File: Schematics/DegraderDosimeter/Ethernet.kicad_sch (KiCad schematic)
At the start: 38 parts, among them J1 RJ45_Amphenol_RJMG1BD3B8K1ANR, U1 LAN8742A, U2 USBLC6-4SC6, U3 H1102NL, Y1 Crystal

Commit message: Set Ethernet PHY crystal value to 25.000 MHz
Y1 carried the generic "Crystal" value with no frequency. The LAN8742A
RMII reference design clocks the PHY from a 25 MHz crystal (X4,
X53T-C20SSA25.000MHz on the ST Nucleo-144 MB1137/MB1364 boards), from
which the PHY derives the 50 MHz RMII_REF_CLK for the MCU. The 30 pF
load capacitors already match.

Co-Authored-By: Claude Opus 5 <noreply@anthropic.com>
Claude-Session: https://claude.ai/code/session_01Ej9hevrS5JU2uwVi6UHQUS
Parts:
- Y1: value Crystal -> 25.000MHz
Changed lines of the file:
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@@
 			)
 		)
-		(property "Value" "Crystal"
+		(property "Value" "25.000MHz"
 			(at 49.234 127.2539 90)
 			(show_name no)

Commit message: Align Ethernet passives with MB1364-H723ZG BOM and fix footprints
Every passive on the sheet carried Capacitor_SMD:C_1206_3216Metric,
including all 22 resistors. Assign real packages matching the
NUCLEO-H723ZG BOM (MB1364-H723ZG-E01), which uses 0402 throughout:

  R1-R22   -> Resistor_SMD:R_0402_1005Metric   (RC0402FR-07* series)
  C1-C9    -> Capacitor_SMD:C_0402_1005Metric
  C10      -> kept at 1206; the 1nF Bob Smith cap is 2kV rated
              (CC1206KKX7RDBB102) and genuinely is a 1206 part
  FB1      -> Inductor_SMD:L_0603_1608Metric   (FCM1608KF-601T03)

Two value corrections from the same BOM:

  R12-R15  50 -> 49R9   centre-tap termination is RC0402FR-0749R9L
  C1, C2   30p -> 5.6p  X4 is an NDK NX2016SA 25MHz 6pF-load crystal,
                        loaded with 5.6pF (CC0402BRNPO9BN5R6), not the
                        30pF used with the older MB1137 crystal

ERC violation count is unchanged at 1445, so no new violations.

Co-Authored-By: Claude Opus 5 <noreply@anthropic.com>
Claude-Session: https://claude.ai/code/session_01Ej9hevrS5JU2uwVi6UHQUS
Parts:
- C1, C2: value 30p -> 5.6p; footprint Capacitor_SMD:C_1206_3216Metric -> Capacitor_SMD:C_0402_1005Metric
- C3, C4, C5, C6, C7, C8, C9: footprint Capacitor_SMD:C_1206_3216Metric -> Capacitor_SMD:C_0402_1005Metric
- FB1: footprint Ferrite_THT:LairdTech_28C0236-0JW-10 -> Inductor_SMD:L_0603_1608Metric
- R1, R10, R11, R16, R17, R18, R19, R2, R20, R21, R22, R3, R4, R5, R6, R7, R8, R9: footprint Capacitor_SMD:C_1206_3216Metric -> Resistor_SMD:R_0402_1005Metric
- R12, R13, R14, R15: value 50 -> 49R9; footprint Capacitor_SMD:C_1206_3216Metric -> Resistor_SMD:R_0402_1005Metric
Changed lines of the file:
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@@
 			)
 		)
-		(property "Footprint" "Capacitor_SMD:C_1206_3216Metric"
+		(property "Footprint" "Resistor_SMD:R_0402_1005Metric"
 			(at 208.026 113.538 0)
 			(hide yes)
@@
 			)
 		)
-		(property "Footprint" "Capacitor_SMD:C_1206_3216Metric"
+		(property "Footprint" "Resistor_SMD:R_0402_1005Metric"
 			(at 33.528 65.024 0)
 			(hide yes)
@@
 			)
 		)
-		(property "Footprint" "Capacitor_SMD:C_1206_3216Metric"
+		(property "Footprint" "Resistor_SMD:R_0402_1005Metric"
 			(at 193.04 113.538 0)
 			(hide yes)
@@
 			)
 		)
-		(property "Footprint" "Capacitor_SMD:C_1206_3216Metric"
+		(property "Footprint" "Capacitor_SMD:C_0402_1005Metric"
 			(at 63.5 39.8272 0)
 			(hide yes)
@@
 			)
 		)
-		(property "Value" "50"
+		(property "Value" "49R9"
 			(at 154.94 36.068 0)
 			(show_name no)
@@
 			)
 		)
-		(property "Footprint" "Capacitor_SMD:C_1206_3216Metric"
+		(property "Footprint" "Resistor_SMD:R_0402_1005Metric"
 			(at 158.242 34.544 0)
 			(hide yes)
@@
 			)
 		)
-		(property "Footprint" "Capacitor_SMD:C_1206_3216Metric"
+		(property "Footprint" "Capacitor_SMD:C_0402_1005Metric"
 			(at 63.5 20.0152 0)
 			(hide yes)
@@
 			)
 		)
-		(property "Value" "30p"
+		(property "Value" "5.6p"
 			(at 34.036 122.682 90)
 			(show_name no)
@@
 			)
 		)
-		(property "Footprint" "Capacitor_SMD:C_1206_3216Metric"
+		(property "Footprint" "Capacitor_SMD:C_0402_1005Metric"
 			(at 37.592 117.3988 0)
 			(hide yes)
@@
 			)
 		)
-		(property "Value" "30p"
+		(property "Value" "5.6p"
 			(at 33.782 138.176 90)
 			(show_name no)
@@
 			)
 		)
-		(property "Footprint" "Capacitor_SMD:C_1206_3216Metric"
+		(property "Footprint" "Capacitor_SMD:C_0402_1005Metric"
 			(at 37.592 133.1468 0)
 			(hide yes)
@@
 			)
 		)
-		(property "Footprint" "Capacitor_SMD:C_1206_3216Metric"
+		(property "Footprint" "Resistor_SMD:R_0402_1005Metric"
 			(at 33.528 68.072 0)
 			(hide yes)
@@
 			)
 		)
-		(property "Footprint" "Capacitor_SMD:C_1206_3216Metric"
+		(property "Footprint" "Resistor_SMD:R_0402_1005Metric"
 			(at 47.498 44.45 0)
 			(hide yes)
@@
 			)
 		)
-		(property "Footprint" "Ferrite_THT:LairdTech_28C0236-0JW-10"
+		(property "Footprint" "Inductor_SMD:L_0603_1608Metric"
 			(at 204.724 23.114 90)
 			(hide yes)
@@
 			)
 		)
-		(property "Footprint" "Capacitor_SMD:C_1206_3216Metric"
+		(property "Footprint" "Resistor_SMD:R_0402_1005Metric"
 			(at 40.386 44.45 0)
 			(hide yes)
@@
 			)
 		)
-		(property "Footprint" "Capacitor_SMD:C_1206_3216Metric"
+		(property "Footprint" "Resistor_SMD:R_0402_1005Metric"
 			(at 33.782 72.898 0)
 			(hide yes)
@@
 			)
 		)
-		(property "Footprint" "Capacitor_SMD:C_1206_3216Metric"
+		(property "Footprint" "Resistor_SMD:R_0402_1005Metric"
 			(at 271.018 106.426 0)
 			(hide yes)
@@
 			)
 		)
-		(property "Footprint" "Capacitor_SMD:C_1206_3216Metric"
+		(property "Footprint" "Resistor_SMD:R_0402_1005Metric"
 			(at 54.864 73.914 0)
 			(hide yes)
@@
 			)
 		)
-		(property "Value" "50"
+		(property "Value" "49R9"
 			(at 133.858 36.322 0)
 			(show_name no)
@@
 			)
 		)
-		(property "Footprint" "Capacitor_SMD:C_1206_3216Metric"
+		(property "Footprint" "Resistor_SMD:R_0402_1005Metric"
 			(at 137.16 34.798 0)
 			(hide yes)
@@
 			)
 		)
-		(property "Footprint" "Capacitor_SMD:C_1206_3216Metric"
+		(property "Footprint" "Resistor_SMD:R_0402_1005Metric"
 			(at 105.664 78.994 0)
 			(hide yes)
@@
 			)
 		)
-		(property "Value" "50"
+		(property "Value" "49R9"
 			(at 148.336 36.068 0)
 			(show_name no)
@@
 			)
 		)
-		(property "Footprint" "Capacitor_SMD:C_1206_3216Metric"
+		(property "Footprint" "Resistor_SMD:R_0402_1005Metric"
 			(at 151.638 34.544 0)
 			(hide yes)
@@
 			)
 		)
-		(property "Footprint" "Capacitor_SMD:C_1206_3216Metric"
+		(property "Footprint" "Resistor_SMD:R_0402_1005Metric"
 			(at 20.32 81.28 0)
 			(hide yes)
@@
 			)
 		)
-		(property "Footprint" "Capacitor_SMD:C_1206_3216Metric"
+		(property "Footprint" "Capacitor_SMD:C_0402_1005Metric"
 			(at 63.5 30.1752 0)
 			(hide yes)
@@
 			)
 		)
-		(property "Footprint" "Capacitor_SMD:C_1206_3216Metric"
+		(property "Footprint" "Capacitor_SMD:C_0402_1005Metric"
 			(at 102.8192 44.958 0)
 			(hide yes)
@@
 			)
 		)
-		(property "Footprint" "Capacitor_SMD:C_1206_3216Metric"
+		(property "Footprint" "Resistor_SMD:R_0402_1005Metric"
 			(at 185.42 113.538 0)
 			(hide yes)
@@
 			)
 		)
-		(property "Footprint" "Capacitor_SMD:C_1206_3216Metric"
+		(property "Footprint" "Resistor_SMD:R_0402_1005Metric"
 			(at 200.66 113.538 0)
 			(hide yes)
@@
 			)
 		)
-		(property "Footprint" "Capacitor_SMD:C_1206_3216Metric"
+		(property "Footprint" "Resistor_SMD:R_0402_1005Metric"
 			(at 257.556 103.886 0)
 			(hide yes)
@@
 			)
 		)
-		(property "Footprint" "Capacitor_SMD:C_1206_3216Metric"
+		(property "Footprint" "Capacitor_SMD:C_0402_1005Metric"
 			(at 122.8852 44.958 0)
 			(hide yes)
@@
 			)
 		)
-		(property "Footprint" "Capacitor_SMD:C_1206_3216Metric"
+		(property "Footprint" "Capacitor_SMD:C_0402_1005Metric"
 			(at 112.9792 44.704 0)
 			(hide yes)
@@
 			)
 		)
-		(property "Footprint" "Capacitor_SMD:C_1206_3216Metric"
+		(property "Footprint" "Resistor_SMD:R_0402_1005Metric"
 			(at 20.32 97.282 0)
 			(hide yes)
@@
 			)
 		)
-		(property "Footprint" "Capacitor_SMD:C_1206_3216Metric"
+		(property "Footprint" "Resistor_SMD:R_0402_1005Metric"
 			(at 36.576 105.664 0)
 			(hide yes)
@@
 			)
 		)
-		(property "Footprint" "Capacitor_SMD:C_1206_3216Metric"
+		(property "Footprint" "Resistor_SMD:R_0402_1005Metric"
 			(at 257.556 93.726 0)
 			(hide yes)
@@
 			)
 		)
-		(property "Value" "50"
+		(property "Value" "49R9"
 			(at 141.224 36.322 0)
 			(show_name no)
@@
 			)
 		)
-		(property "Footprint" "Capacitor_SMD:C_1206_3216Metric"
+		(property "Footprint" "Resistor_SMD:R_0402_1005Metric"
 			(at 144.526 34.798 0)
 			(hide yes)
@@
 			)
 		)
-		(property "Footprint" "Capacitor_SMD:C_1206_3216Metric"
+		(property "Footprint" "Resistor_SMD:R_0402_1005Metric"
 			(at 54.102 44.45 0)
 			(hide yes)
@@
 			)
 		)
-		(property "Footprint" "Capacitor_SMD:C_1206_3216Metric"
+		(property "Footprint" "Capacitor_SMD:C_0402_1005Metric"
 			(at 221.4372 35.306 0)
 			(hide yes)

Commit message: Set Ethernet ferrite bead value to 600R@100MHz
FB1 carried the placeholder value "FerriteBead_Small" with no impedance
specified. It matches L1 on the MB1364 Ethernet sheet, which feeds the
PHY supply from 3V3 and is a TAI-TECH FCM1608KF-601T03, 600R@100MHz
+/-25%, 350mA, 0603. The 0603 footprint set in the previous commit is
already correct for that part.

Co-Authored-By: Claude Opus 5 <noreply@anthropic.com>
Claude-Session: https://claude.ai/code/session_01Ej9hevrS5JU2uwVi6UHQUS
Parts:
- FB1: value FerriteBead_Small -> 600R@100MHz
- R1: value R_Small_US -> 33
- Y1: footprint Crystal:Crystal_SMD_Abracon_ABM10-4Pin_2.5x2.0mm -> Crystal:Crystal_SMD_Abracon_ABM3-2Pin_5.0x3.2mm_HandSoldering
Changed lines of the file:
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@@
 			)
 		)
-		(property "Footprint" "Crystal:Crystal_SMD_Abracon_ABM10-4Pin_2.5x2.0mm"
+		(property "Footprint" "Crystal:Crystal_SMD_Abracon_ABM3-2Pin_5.0x3.2mm_HandSoldering"
 			(at 44.704 125.984 0)
 			(hide yes)
@@
 			)
 		)
-		(property "Value" "FerriteBead_Small"
+		(property "Value" "600R@100MHz"
 			(at 186.182 23.114 0)
 			(show_name no)
@@
 			)
 		)
-		(property "Value" "R_Small_US"
+		(property "Value" "33"
 			(at 36.576 109.982 90)
 			(show_name no)

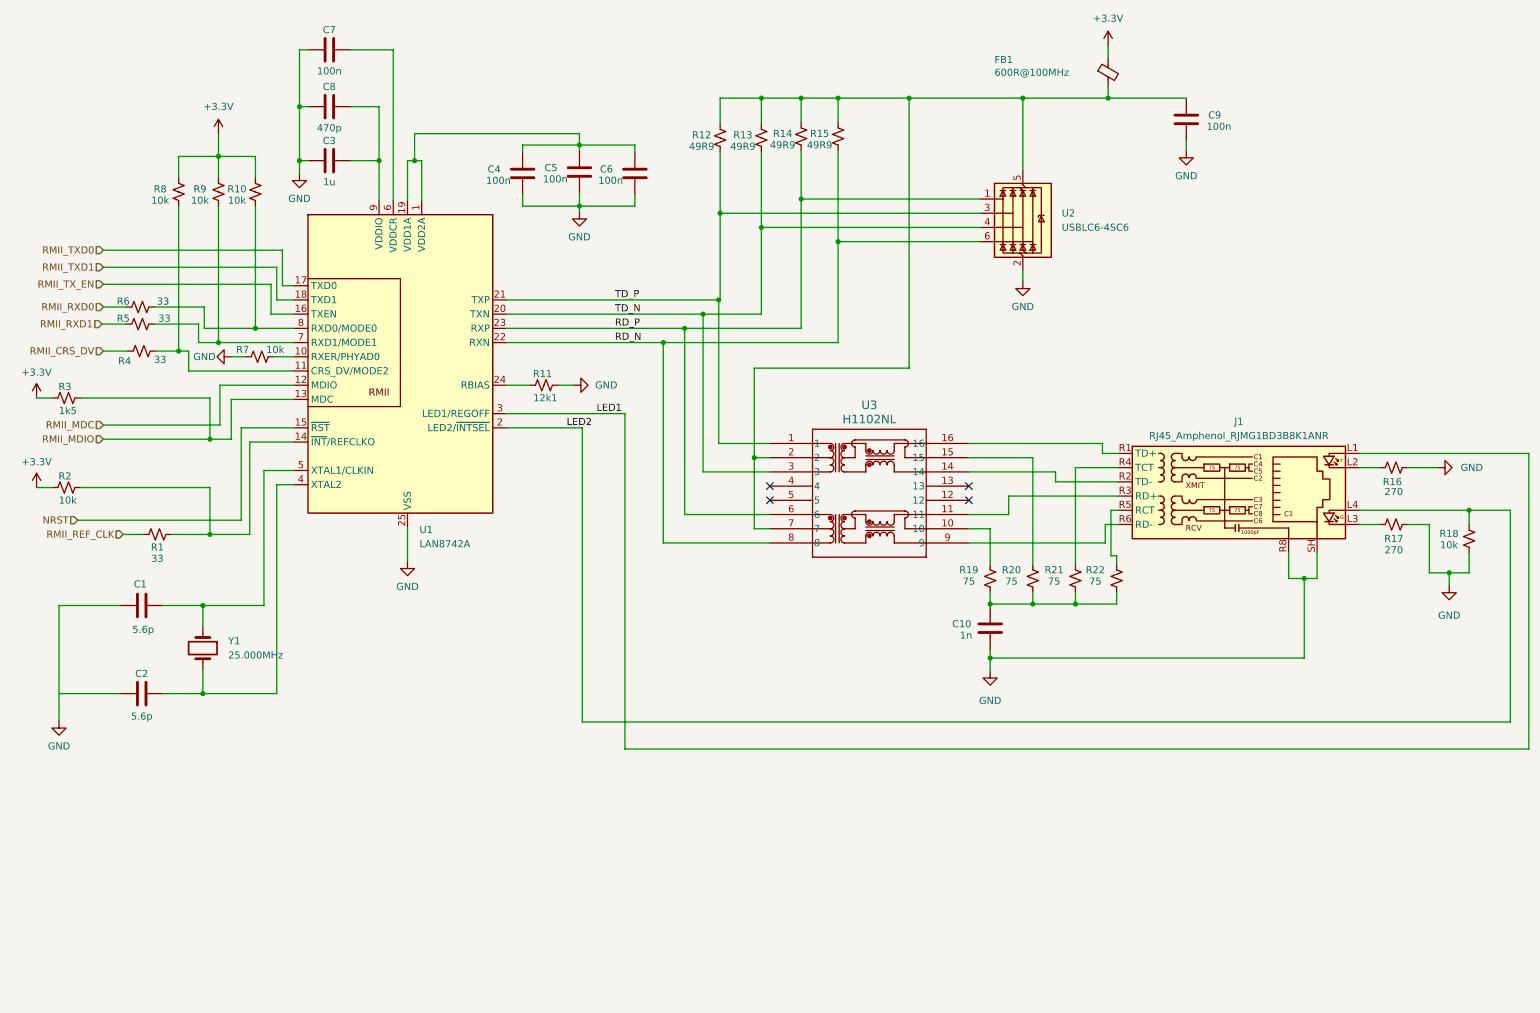
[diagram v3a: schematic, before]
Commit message: Replace MagJack with the MB1364 RJ45 and remove the double magnetics
J1 was an Amphenol RJMG1BD3B8K1ANR, a MagJack with integrated magnetics,
sitting in series after U3 (H1102NL). Two transformers back to back
attenuate the signal and break the 100 ohm match, so the link would not
have come up.

Replace it with the jack ST actually fits, CN14 = Dongguan Keyouda
KRJ-CB4.2GYZNL, a plain shielded RJ45 with two LEDs and no magnetics,
drawn with Connector:RJ45_LED_Shielded. U3 now provides the only
magnetics stage, matching the MB1364 Ethernet sheet.

Connectivity, verified against the exported netlist:

  U3.16 -> J1.1 TX+      U3.14 -> J1.2 TX-
  U3.11 -> J1.3 RX+      U3.9  -> J1.6 RX-
  J1.4 + J1.5 -> R21     J1.7 + J1.8 -> R22   (unused pairs)
  R19/R20 (secondary CTs) + R21/R22 -> C10 -> GND   (Bob Smith)
  J1.9/10 LEDs via R16, J1.11/12 via R17/R18, J1.SH -> GND

Add a KRJ-CB4.2GYZNL footprint built from ST's MB1364C production drill
data (CN14 at 44.3686, 7.9499): eight 0.70mm signal holes on a 1.02mm
pitch, four 0.70mm LED holes at +/-4.77 and +/-7.06mm, and two 0.70 x
1.50mm plated shield slots at +/-8.04mm. Gerber Y is negated for KiCad.

NOTE: the drill data fixes hole positions but not pin numbering. Pin 1
is placed at the leftmost signal hole and LED pins 9-12 left to right;
verify both against the KRJ-CB4.2GYZNL datasheet before ordering, along
with the body outline, which is not derivable from drill data.

Co-Authored-By: Claude Opus 5 <noreply@anthropic.com>
Claude-Session: https://claude.ai/code/session_01Ej9hevrS5JU2uwVi6UHQUS
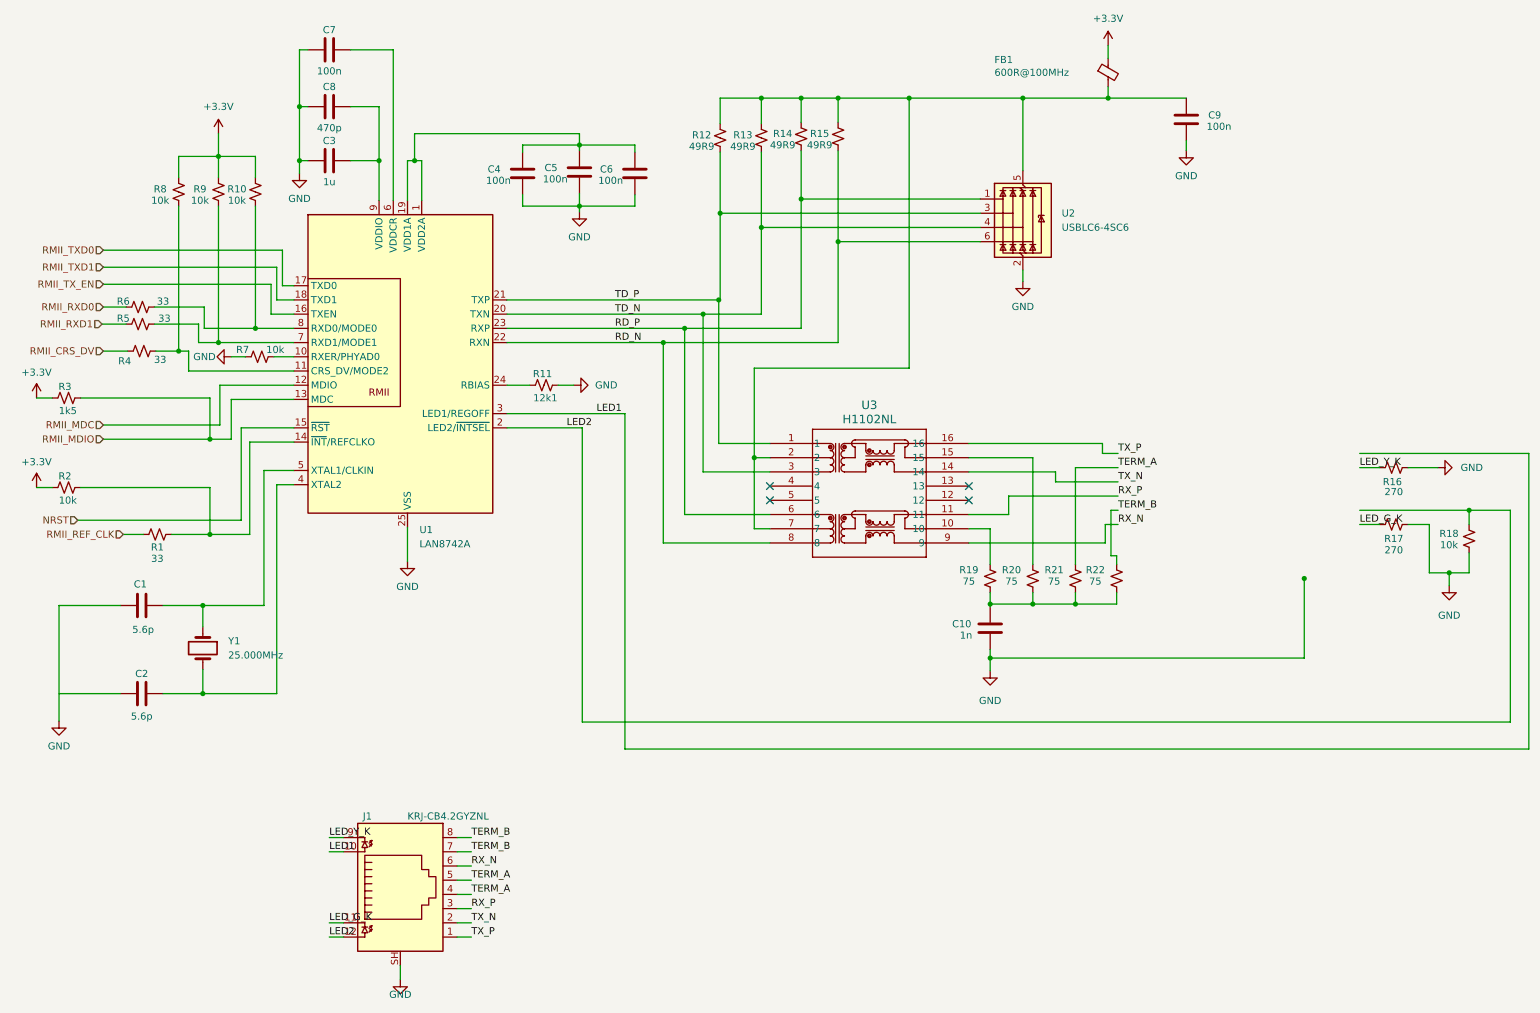
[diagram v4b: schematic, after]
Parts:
- removed J1: RJ45_Amphenol_RJMG1BD3B8K1ANR, Connector_RJ:RJ45_Pulse_JK0654219NL_Horizontal, symbol Connector:RJ45_Amphenol_RJMG1BD3B8K1ANR
- added J1: KRJ-CB4.2GYZNL, KRJ-CB4.2GYZNL:KRJ-CB4.2GYZNL, symbol Connector:RJ45_LED_Shielded
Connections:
- net GND: now also J1.SH
- net LED1: now also J1.10
- net LED2: now also J1.12
- net TERM_B: now reaches R22.1
- net TERM_B: now also J1.7, J1.8
- net RX_P: now reaches U3.11
- net RX_P: now also J1.3
- net TX_N: now reaches U3.14
- net TX_N: now also J1.2
- net TX_P: now reaches U3.16
- net TX_P: now also J1.1
- net RX_N: now reaches U3.9
- net RX_N: now also J1.6
- net LED_Y_K: now reaches R16.1
- net LED_Y_K: now also J1.9
- net LED_G_K: now reaches R17.2
- net LED_G_K: now also J1.11
- net TERM_A: now reaches R21.1
- net TERM_A: now also J1.4, J1.5

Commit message: Move Y1 to the NX2016SA 4-pad crystal and ground the C2 load cap
Y1 was a 2-pin Device:Crystal on a 5.0x3.2mm hand-solder footprint. The
MB1364 BOM fits an NDK NX2016SA 25MHz, 6pF load, +/-20ppm (X4), which is
a 4-pad part: two terminals plus two case-ground pads. Switch to
Device:Crystal_GND24 with Crystal:Crystal_SMD_2016-4Pin_2.0x1.6mm and
tie the case pads to GND.

Pins 1 and 3 of Crystal_GND24 sit exactly where the 2-pin symbol's pins
were, so the existing XTAL1/XTAL2 wiring is unchanged:

  Y1.1 -> U1.5 XTAL1/CLKIN, C1.2
  Y1.3 -> U1.4 XTAL2, C2.2
  Y1.2, Y1.4 (case) -> GND

C1/C2 stay at 5.6pF, which is the right load for a 6pF crystal
(CC0402BRNPO9BN5R6 on the ST board) and needs no change.

Also fix C2 pad 1, which was floating: one of the two crystal load caps
had no ground return, so the oscillator had no proper load. It is now on
GND alongside C1 pad 1.

Co-Authored-By: Claude Opus 5 <noreply@anthropic.com>
Claude-Session: https://claude.ai/code/session_01Ej9hevrS5JU2uwVi6UHQUS
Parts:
- Y1: footprint Crystal:Crystal_SMD_Abracon_ABM3-2Pin_5.0x3.2mm_HandSoldering -> Crystal:Crystal_SMD_2016-4Pin_2.0x1.6mm; symbol Device:Crystal -> Device:Crystal_GND24
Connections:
- net GND: now also C2.1, Y1.2 (G), Y1.4 (G)
- net at C2.2, U1.4 (XTAL2): now also Y1.3; no longer Y1.2
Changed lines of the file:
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@@
 	)
 	(symbol
-		(lib_id "Device:Crystal")
+		(lib_id "Device:Crystal_GND24")
 		(at 44.704 125.984 270)
 		(unit 1)
@@
 			)
 		)
-		(property "Footprint" "Crystal:Crystal_SMD_Abracon_ABM3-2Pin_5.0x3.2mm_HandSoldering"
+		(property "Footprint" "Crystal:Crystal_SMD_2016-4Pin_2.0x1.6mm"
 			(at 44.704 125.984 0)
 			(hide yes)
@@
 			)
 		)
+		(pin "1"
+		)
 		(pin "2"
 		)
-		(pin "1"
+		(pin "3"
+		)
+		(pin "4"
 		)
 		(instances
@@
 					(unit 1)
 				)
+			)
+		)
+	)
+	(wire
+		(pts
+			(xy 39.624 125.984) (xy 34.544 125.984)
+		)
+		(stroke
+			(width 0)
+			(type default)
+		)
+	)
+	(symbol
+		(lib_id "power:GND")
+		(at 34.544 125.984 0)
+		(unit 1)
+		(body_style 1)
+		(exclude_from_sim no)
+		(in_bom yes)
+		(on_board yes)
+		(in_pos_files yes)
+		(dnp no)
+		(fields_autoplaced yes)
+		(property "Reference" "#PWR0102"
+			(at 34.544 124.984 0)
+			(hide yes)
+			(show_name no)
+			(do_not_autoplace no)
+			(effects
+				(font
+					(size 1.27 1.27)
+				)
+			)
+		)
+		(property "Value" "GND"
+			(at 34.544 129.184 0)
+			(show_name no)
+			(do_not_autoplace no)
+			(effects
+				(font
+					(size 1.27 1.27)
+				)
+			)
+		)
+		(pin "1"
+		)
+		(instances
+			(project "DegraderDosimeter"
+				(path "/f3c83d46-b432-4960-ae55-27eb620ca6d0/29cc5153-f00a-421d-a7d0-f0b15c27dbc7"
+					(reference "#PWR0102")
+					(unit 1)
+				)
+			)
+		)
+	)
+	(wire
+		(pts
+			(xy 29.972 134.112) (xy 29.972 139.192)
+		)
+		(stroke
+			(width 0)
+			(type default)
+		)
+	)
+	(symbol
+		(lib_id "power:GND")
+		(at 29.972 139.192 0)
+		(unit 1)
+		(body_style 1)
+		(exclude_from_sim no)
+		(in_bom yes)
+		(on_board yes)
+		(in_pos_files yes)
+		(dnp no)
+		(fields_autoplaced yes)
+		(property "Reference" "#PWR0103"
+			(at 29.972 138.192 0)
+			(hide yes)
+			(show_name no)
+			(do_not_autoplace no)
+			(effects
+				(font
+					(size 1.27 1.27)
+				)
+			)
+		)
+		(property "Value" "GND"
+			(at 29.972 142.392 0)
+			(show_name no)
+			(do_not_autoplace no)
+			(effects
+				(font
+					(size 1.27 1.27)
+				)
+			)
+		)
+		(pin "1"
+		)
+		(instances
+			(project "DegraderDosimeter"
+				(path "/f3c83d46-b432-4960-ae55-27eb620ca6d0/29cc5153-f00a-421d-a7d0-f0b15c27dbc7"
+					(reference "#PWR0103")
+					(unit 1)
+				)
